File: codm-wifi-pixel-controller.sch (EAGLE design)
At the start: 46 parts, among them U1 AP62XXX-TSOT26, U2 REG710NA-5/250, U3 SN74AHCT125PWR, U4 ESP-WROOM-32

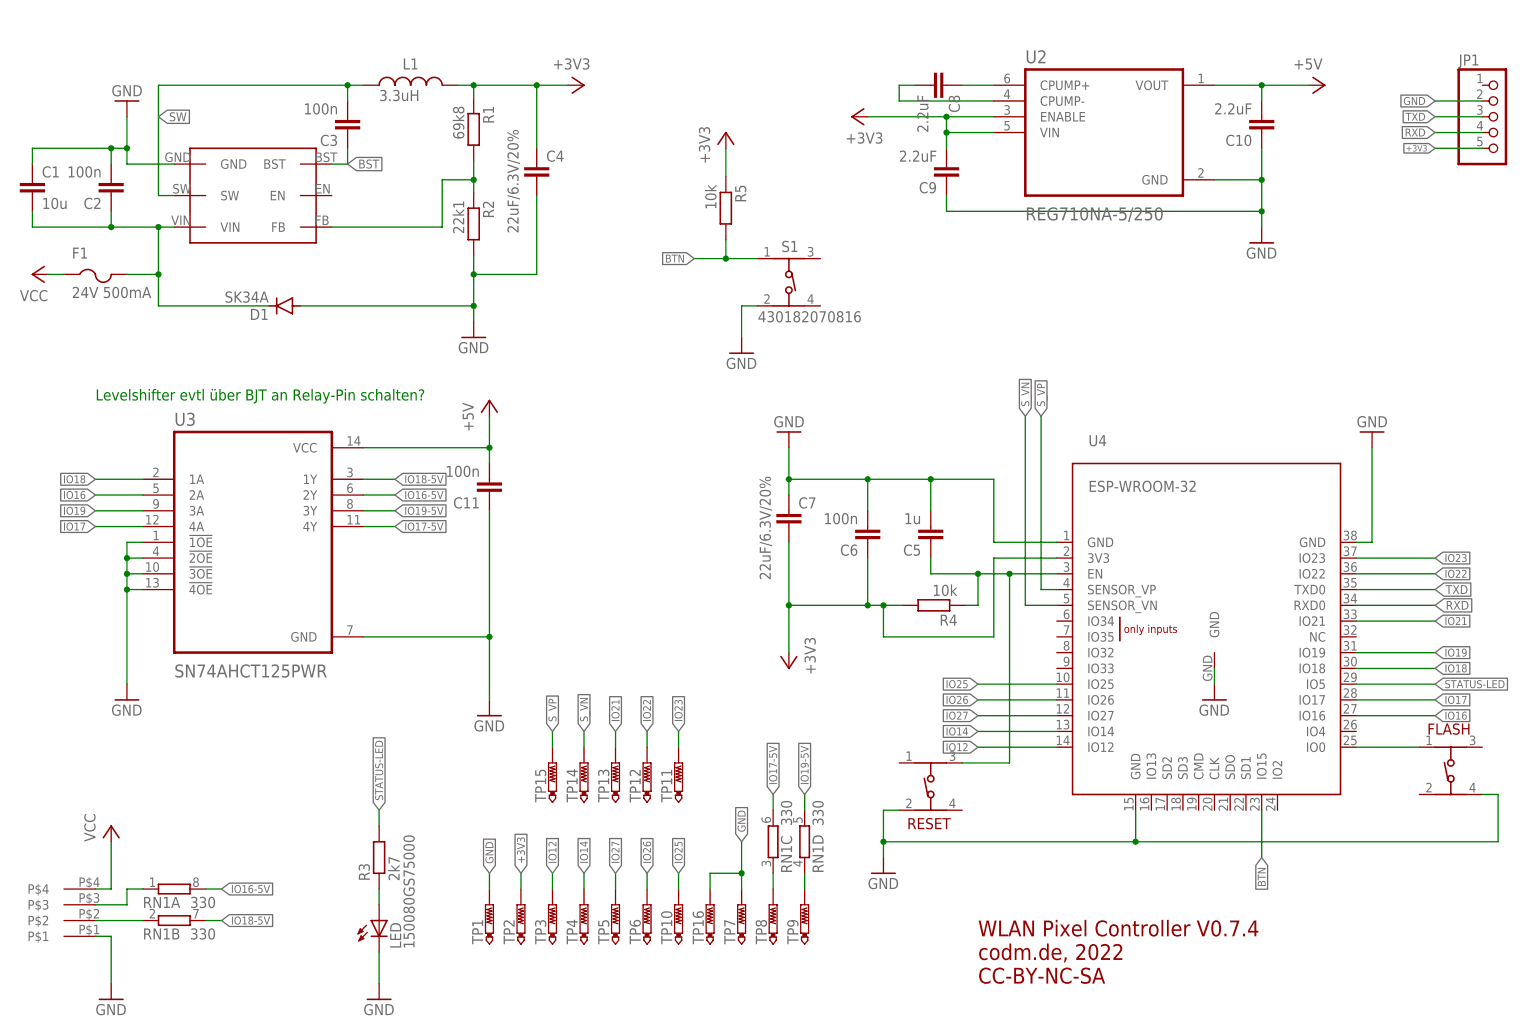
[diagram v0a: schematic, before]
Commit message: better esp32 footprint, minor rearangements
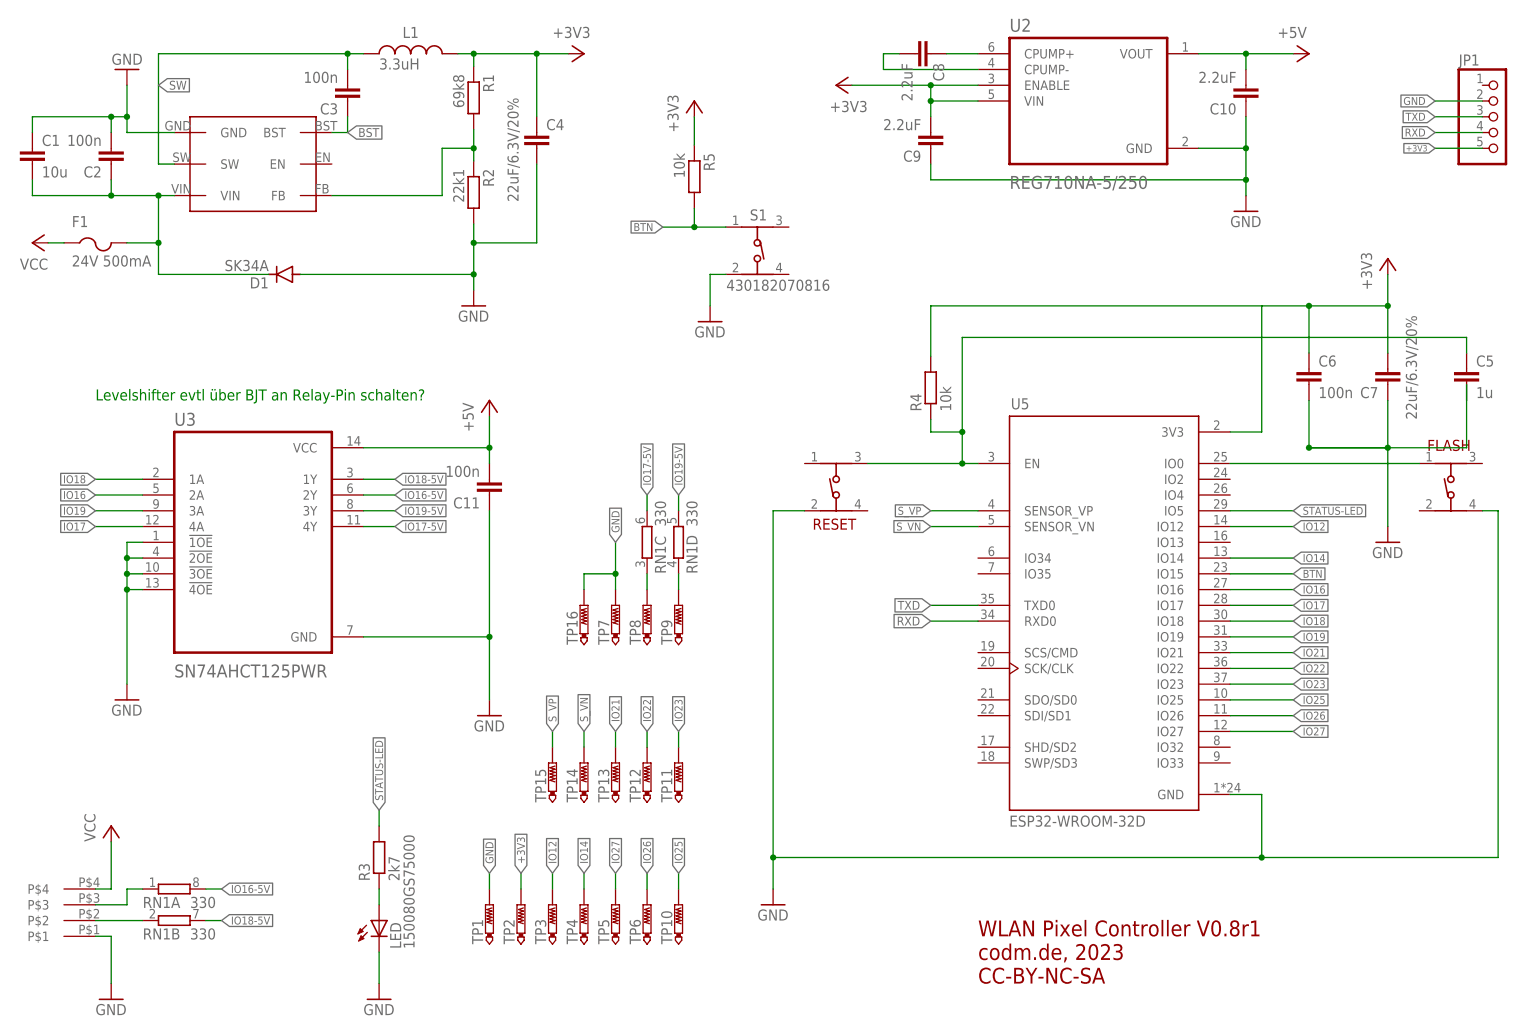
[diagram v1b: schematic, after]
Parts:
- removed U4: ESP-WROOM-32, esp32:ESP-WROOM-32
- added U5: ESP32-WROOM-32D, ESP32-WROOM-32D:ESP32-WROOM-32D
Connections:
- net +3V3: now also U5.3V3; no longer U4.3V3
- net BTN: now also U5.IO15; no longer U4.IO15
- net GND: now also U5.GND; no longer U4.GND, U4.GND@1, U4.GND@15, U4.GND@38
- net GPIO0: now also U5.IO0; no longer U4.IO0
- net IO12: now also U5.IO12; no longer U4.IO12
- net IO14: now also U5.IO14; no longer U4.IO14
- net IO16: now also U5.IO16; no longer U4.IO16
- net IO17: now also U5.IO17; no longer U4.IO17
- net IO18: now also U5.IO18; no longer U4.IO18
- net IO19: now also U5.IO19; no longer U4.IO19
- net IO21: now also U5.IO21; no longer U4.IO21
- net IO22: now also U5.IO22; no longer U4.IO22
- net IO23: now also U5.IO23; no longer U4.IO23
- net IO25: now also U5.IO25; no longer U4.IO25
- net IO26: now also U5.IO26; no longer U4.IO26
- net IO27: now also U5.IO27; no longer U4.IO27
- net RESET: now also U5.EN; no longer U4.EN
- net RXD: now also U5.RXD0; no longer U4.RXD0
- net STATUS-LED: now also U5.IO5; no longer U4.IO5
- net S_VN: now also U5.SENSOR_VN; no longer U4.SENSOR_VN
- net S_VP: now also U5.SENSOR_VP; no longer U4.SENSOR_VP
- net TXD: now also U5.TXD0; no longer U4.TXD0
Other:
- note added: "WLAN Pixel Controller V0.8r1 codm.de, 2023 CC-BY-NC-SA"
- note removed: "WLAN Pixel Controller V0.7.4 codm.de, 2022 CC-BY-NC-SA"
- moved on the sheet: C1, C10, C2, C3, C4, C5, C6, C7, C8, C9, D1, F1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

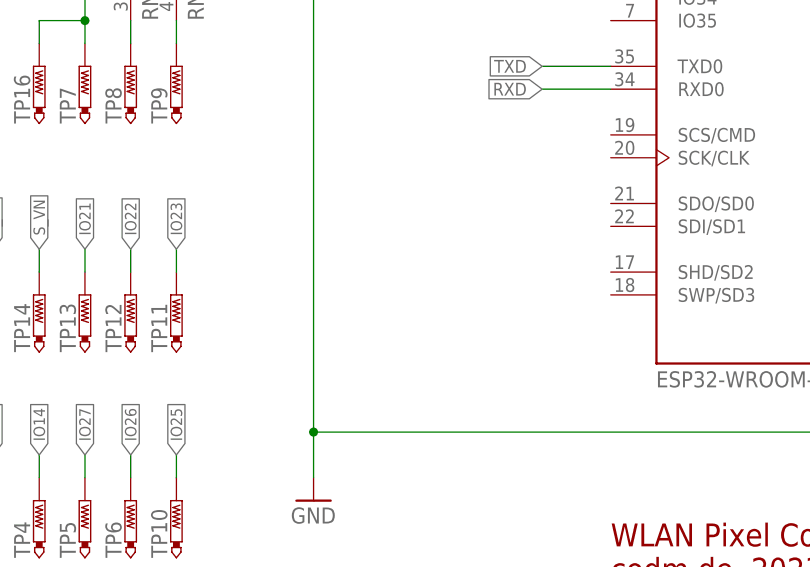
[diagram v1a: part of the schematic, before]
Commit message: better fiducials
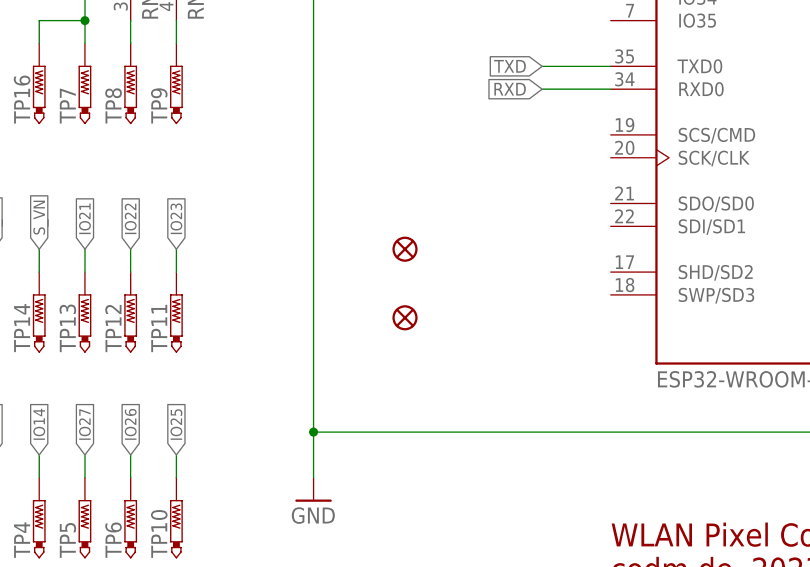
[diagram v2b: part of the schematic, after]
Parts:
- added FD1, FD2: FIDUCIAL1X2, SparkFun-Aesthetics:FIDUCIAL1X2
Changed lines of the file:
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@@
 <part name="TP16" library="testpad" library_urn="urn:adsk.eagle:library:385" deviceset="PTR1" device="TP14R" package3d_urn="urn:adsk.eagle:package:27966/1" value="PTR1TP14R"/>
 <part name="U5" library="ESP32-WROOM-32D" deviceset="ESP32-WROOM-32D" device="" override_package3d_urn="urn:adsk.eagle:package:39135792/2" override_package_urn="urn:adsk.eagle:footprint:39135793/1"/>
+<part name="FD1" library="SparkFun-Aesthetics" library_urn="urn:adsk.eagle:library:507" deviceset="FIDUCIAL" device="1X2" package3d_urn="urn:adsk.eagle:package:37108/1"/>
+<part name="FD2" library="SparkFun-Aesthetics" library_urn="urn:adsk.eagle:library:507" deviceset="FIDUCIAL" device="1X2" package3d_urn="urn:adsk.eagle:package:37108/1"/>
 </parts>
 <sheets>
@@
 <attribute name="VALUE" x="167.5933" y="37.9919" size="1.778" layer="96"/>
 </instance>
+<instance part="FD1" gate="G$1" x="139.7" y="53.34" smashed="yes"/>
+<instance part="FD2" gate="G$1" x="139.7" y="45.72" smashed="yes"/>
 </instances>
 <busses>
